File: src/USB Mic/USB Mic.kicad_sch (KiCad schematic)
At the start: 12 parts, among them IC1 ADUM3160BRWZ-RL, J1 GT-USB-7010ASV

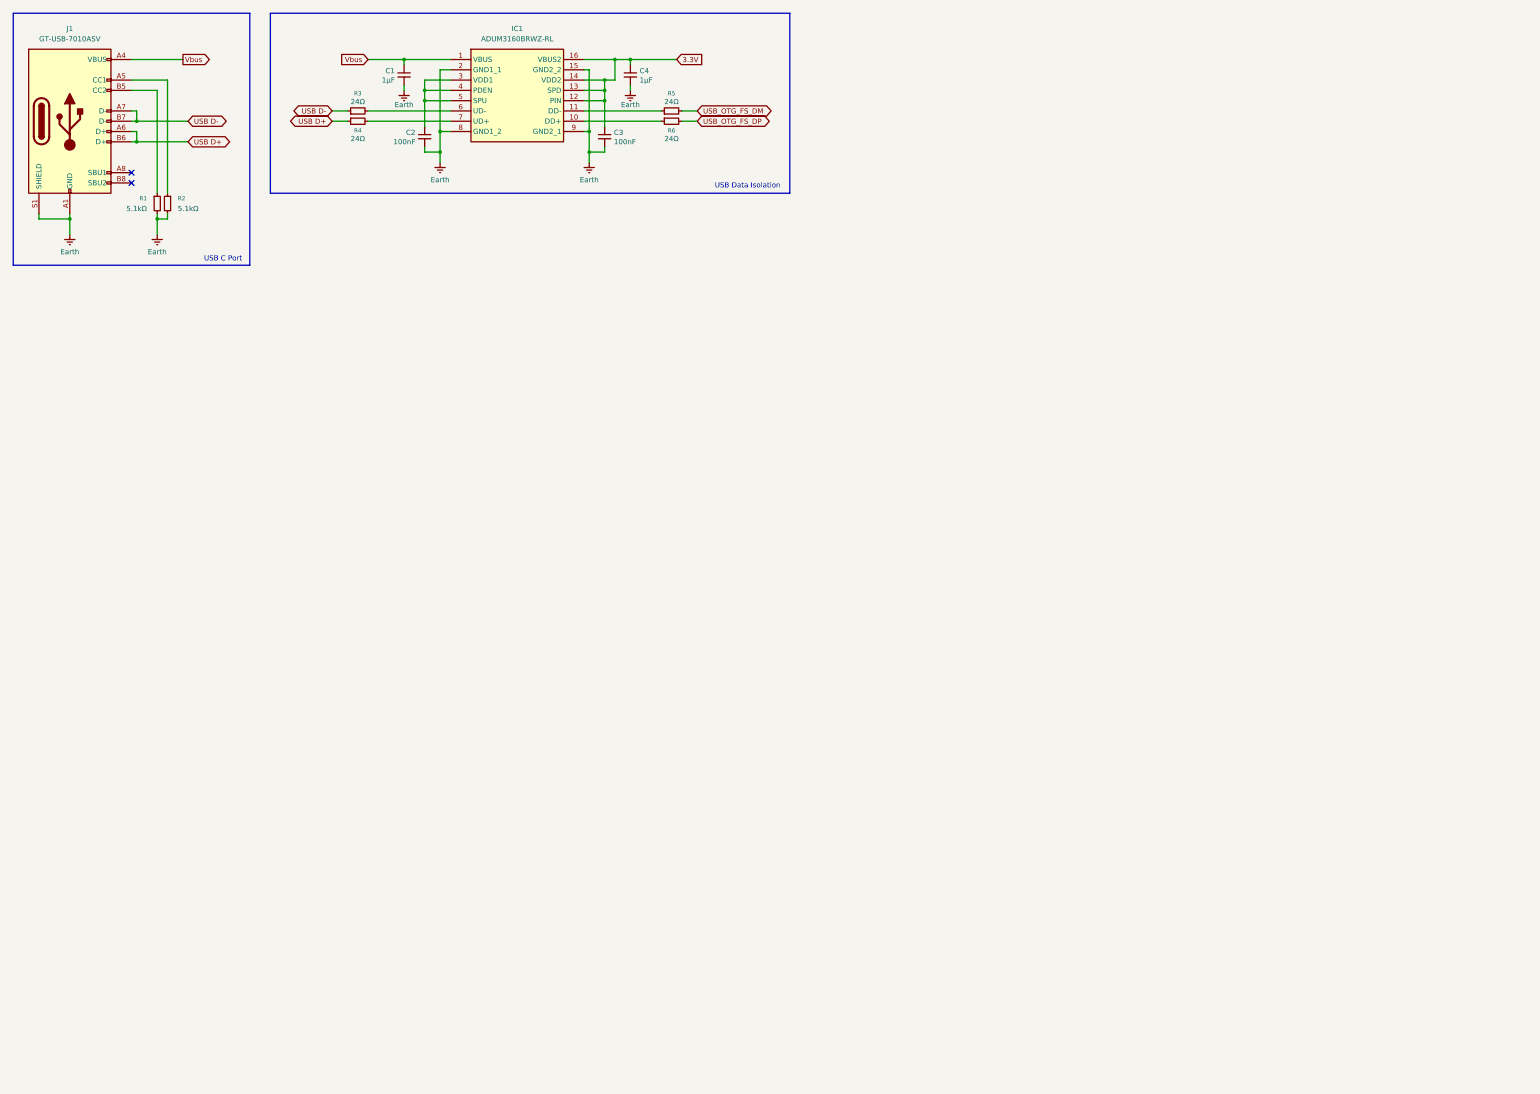
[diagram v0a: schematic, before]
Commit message: Update Rev.4 Schematic
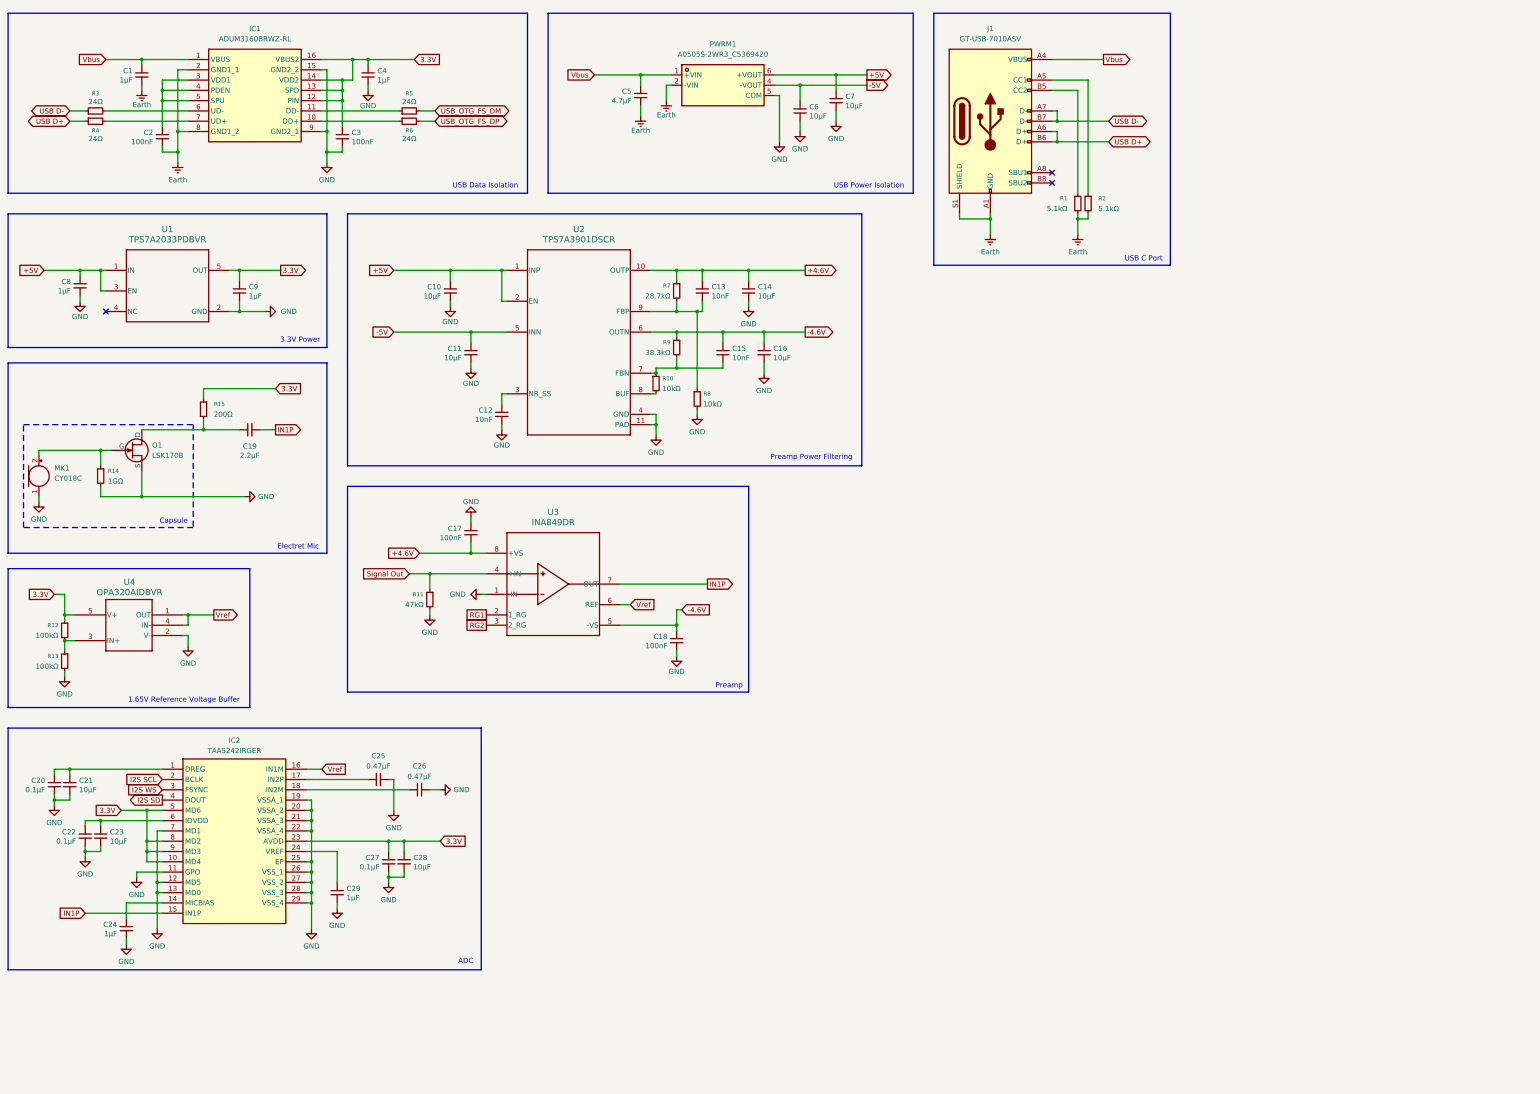
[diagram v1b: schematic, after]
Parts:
- added C10, C11, C14, C16, C21, C23, C28, C6, C7: 10µF, symbol Device:C_Small
- added C12, C13, C15: 10nF, symbol Device:C_Small
- added C17, C18: 100nF, symbol Device:C_Small
- added C19: 2.2µF, symbol Device:C_Small
- added C20, C22, C27: 0.1µF, symbol Device:C_Small
- added C24, C29, C8, C9: 1µF, symbol Device:C_Small
- added C25, C26: 0.47µF, symbol Device:C_Small
- added C5: 4.7µF, symbol Device:C_Small
- added IC2: TAA5242IRGER, footprints:TAA5242IRGER, symbol TAA5242IRGER:TAA5242IRGER
- added MK1: CY018C, symbol Device:Microphone
- added PWRM1: A0505S-2WR3_C5369420, easyeda2kicad:PWRM-TH_HLK-AXXXXS-2WR3, symbol A0505S-2WR3:A0505S-2WR3_C5369420
- added Q1: LSK170B, symbol Simulation_SPICE:NJFET
- added R10, R8: 10kΩ, symbol Device:R_Small
- added R11: 47kΩ, symbol Device:R_Small
- added R12, R13: 100kΩ, symbol Device:R_Small
- added R14: 1GΩ, symbol Device:R_Small
- added R15: 200Ω, symbol Device:R_Small
- added R7: 28.7kΩ, symbol Device:R_Small
- added R9: 38.3kΩ, symbol Device:R_Small
- added U1: TPS7A2033PDBVR, footprints:DBV0005A-IPC_A, symbol TPS7A2033PDBVR:TPS7A2033PDBVR
- added U2: TPS7A3901DSCR, footprints:DSC0010J_NV, symbol TPS7A3901DSCR:TPS7A3901DSCR
- added U3: INA849DR, D0008A-IPC_A, symbol INA849DR:INA849DR
- added U4: OPA320AIDBVR, footprints:DBV5, symbol OPA320AIDBVR:OPA320AIDBVR
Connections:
- net 3.3V: now also C27.1, C28.1, C9.1, IC2.10 (MD4), IC2.23 (AVDD), IC2.5 (MD6), IC2.8 (MD2), IC2.9 (MD3), R12.1, R15.1, U1.5 (OUT), U4.5 (V+)
- net Earth: now also C5.2, PWRM1.2 (-VIN); no longer C3.2, C4.2, IC1.15 (GND2_2), IC1.9 (GND2_1)
- net Vbus: now also C5.1, PWRM1.1 (+VIN)
- new net: C15.2, R10.1, R9.2, U2.7 (FBN)
- new net: R10.2, U2.8 (BUF)
- new net: C12.1, U2.3 (NR_SS)
- new net: C29.1, IC2.24 (VREF)
- new net: MK1.2 (+), Q1.2 (G), R14.1
- new net: C13.2, R7.2, R8.1, U2.9 (FBP)
- new net: C25.1, IC2.17 (IN2P)
- new net: C20.1, C21.1, IC2.1 (DREG)
- new net: C22.1, C23.1, IC2.6 (IOVDD)
- new net: C24.1, IC2.14 (MICBIAS)
- new net: C26.2, IC2.18 (IN2M)
- new net: R12.2, R13.1, U4.3 (IN+)
- new net: C19.1, Q1.1 (D), R15.2
- new net +4.6V: C13.1, C14.1, C17.2, R7.1, U2.10 (OUTP), U3.8 (+VS)
- new net +5V: C10.1, C7.1, C8.1, PWRM1.6 (+VOUT), U1.1 (IN), U1.3 (EN), U2.1 (INP), U2.2 (EN)
- new net -4.6V: C15.1, C16.1, C18.1, R9.1, U2.6 (OUTN), U3.5 (-VS)
- new net -5V: C11.1, C6.1, PWRM1.4 (-VOUT), U2.5 (INN)
- new net GND: C10.2, C11.2, C12.2, C14.2, C16.2, C17.1, C18.2, C20.2, C21.2, C22.2, C23.2, C24.2, C25.2, C26.1, C27.2, C28.2, C29.2, C3.2, C4.2, C6.2, C7.2, C8.2, C9.2, IC1.15 (GND2_2), IC1.9 (GND2_1), IC2.11 (GPO), IC2.12 (MD5), IC2.13 (MD0), IC2.19 (VSSA_1), IC2.20 (VSSA_2), IC2.21 (VSSA_3), IC2.22 (VSSA_4), IC2.25 (EP), IC2.26 (VSS_1), IC2.27 (VSS_2), IC2.28 (VSS_3), IC2.29 (VSS_4), IC2.7 (MD1), MK1.1 (-), PWRM1.5 (COM), Q1.3 (S), R11.2, R13.2, R14.2, R8.2, U1.2 (GND), U2.11 (PAD), U2.4 (GND), U3.1 (-IN), U4.2 (V-)
- new net I2S SCL: IC2.2 (BCLK)
- new net I2S SD: IC2.4 (DOUT)
- new net I2S WS: IC2.3 (FSYNC)
- new net IN1P: C19.2, IC2.15 (IN1P), U3.7 (OUT)
- new net RG1: U3.2 (1_RG)
- new net RG2: U3.3 (2_RG)
- new net Signal Out: R11.1, U3.4 (+IN)
- new net Vref: IC2.16 (IN1M), U3.6 (REF), U4.1 (OUT), U4.4 (IN-)
- no-connect marks 2 -> 3
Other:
- note added: "1.65V Reference Voltage Buffer"
- note added: "3.3V Power"
- note added: "ADC"
- note added: "Capsule"
- note added: "Electret Mic"
- note added: "Preamp"
- note added: "Preamp Power Filtering"
- note added: "USB Power Isolation"
- moved on the sheet: C1, C2, C3, C4, IC1, J1, R1, R2, R3, R4, R5, R6

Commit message: Upload SPICE and update schematic
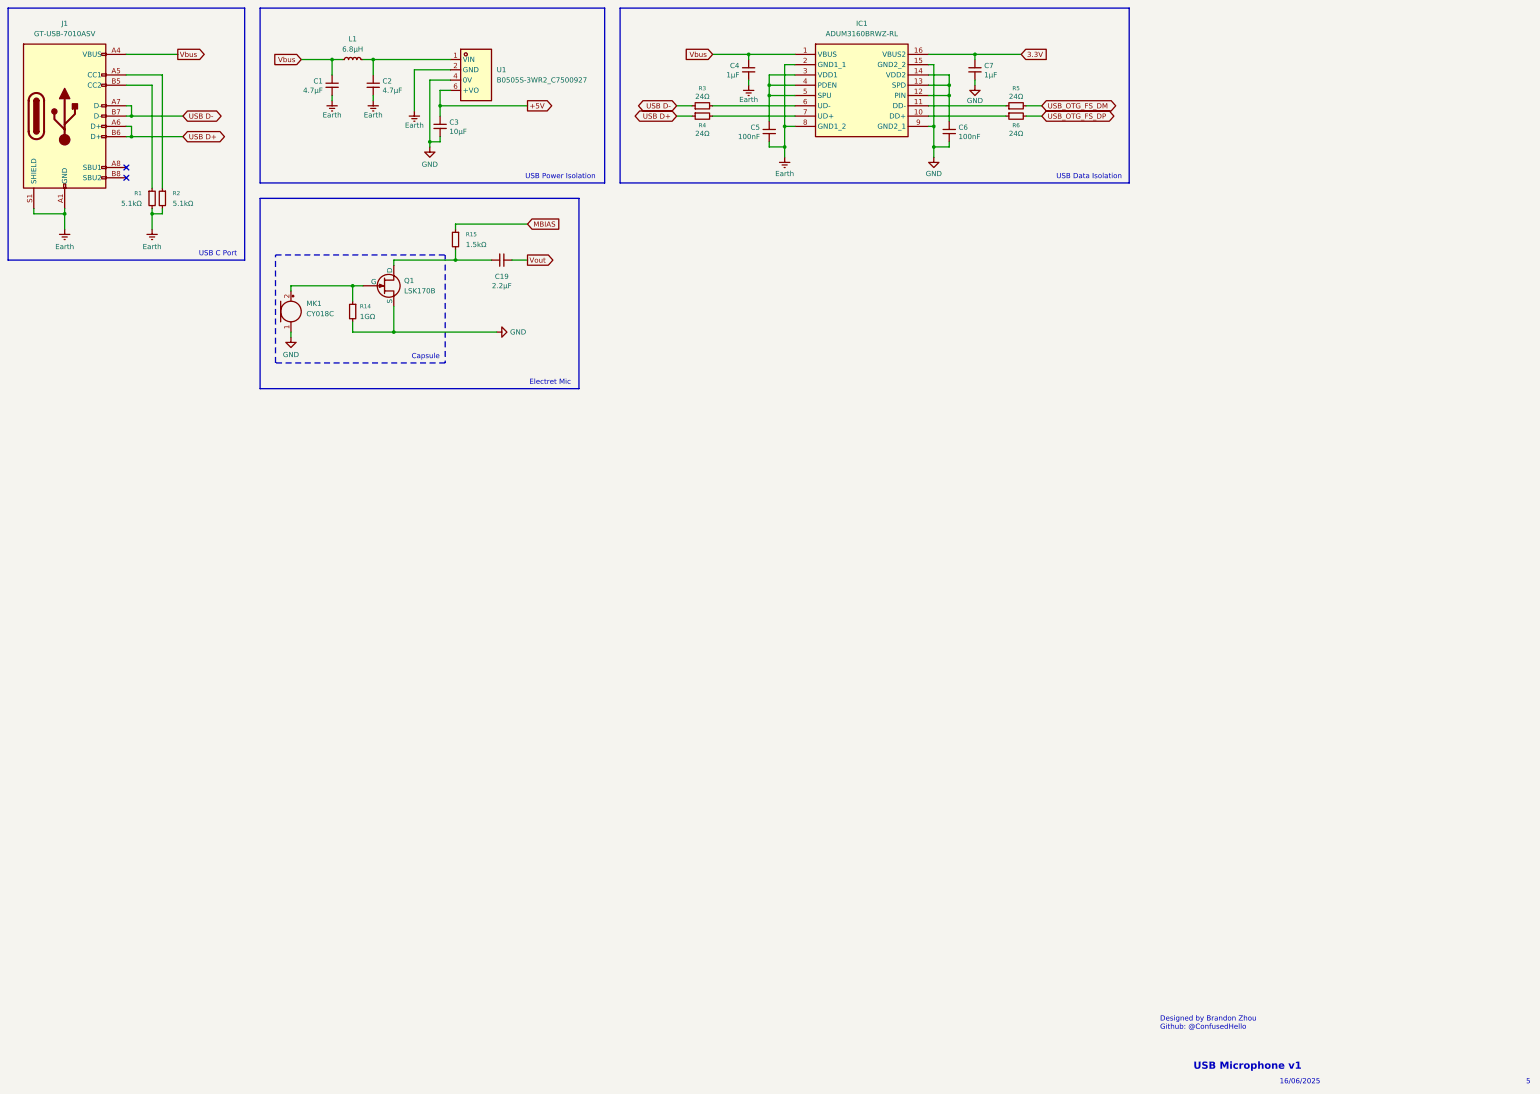
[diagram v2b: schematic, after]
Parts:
- removed C1, C24, C29, C8, C9: 1µF, symbol Device:C_Small
- removed C10, C11, C14, C16, C21, C23, C28, C7: 10µF, symbol Device:C_Small
- removed C12, C13, C15: 10nF, symbol Device:C_Small
- removed C17, C18: 100nF, symbol Device:C_Small
- removed C20, C22, C27: 0.1µF, symbol Device:C_Small
- removed C25, C26: 0.47µF, symbol Device:C_Small
- removed IC2: TAA5242IRGER, footprints:TAA5242IRGER, symbol TAA5242IRGER:TAA5242IRGER
- removed PWRM1: A0505S-2WR3_C5369420, easyeda2kicad:PWRM-TH_HLK-AXXXXS-2WR3, symbol A0505S-2WR3:A0505S-2WR3_C5369420
- removed R10, R8: 10kΩ, symbol Device:R_Small
- removed R11: 47kΩ, symbol Device:R_Small
- removed R12, R13: 100kΩ, symbol Device:R_Small
- removed R7: 28.7kΩ, symbol Device:R_Small
- removed R9: 38.3kΩ, symbol Device:R_Small
- removed U1: TPS7A2033PDBVR, footprints:DBV0005A-IPC_A, symbol TPS7A2033PDBVR:TPS7A2033PDBVR
- removed U2: TPS7A3901DSCR, footprints:DSC0010J_NV, symbol TPS7A3901DSCR:TPS7A3901DSCR
- removed U3: INA849DR, D0008A-IPC_A, symbol INA849DR:INA849DR
- removed U4: OPA320AIDBVR, footprints:DBV5, symbol OPA320AIDBVR:OPA320AIDBVR
- added C4: 1µF, symbol Device:C_Small
- added C5: 100nF, symbol Device:C_Small
- added L1: 6.8µH, footprints:IND-SMD_L4.0-W4.0_YHNR4020, symbol Device:L_Small
- added U1: B0505S-3WR2_C7500927, easyeda2kicad:PWRM-TH_BXXXXS-3WR2, symbol B0505S-3WR2:B0505S-3WR2_C7500927
- C2: value 100nF -> 4.7µF
- C3: value 100nF -> 10µF
- C6: value 10µF -> 100nF
- R15: value 200Ω -> 1.5kΩ
- renumbered C5 to C1, C4 to C7
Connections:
- net +5V: now also C3.1, U1.6 (+VO)
- net 3.3V: no longer C3.1, IC1.12 (PIN), IC1.13 (SPD), IC1.14 (VDD2), R15.1
- net Earth: now also C4.2, C5.2, U1.2 (GND)
- net GND: now also U1.4 (0V)
- net Vbus: now also C4.1, L1.1
- net at IC1.3 (VDD1), IC1.4 (PDEN), IC1.5 (SPU): now also C5.1; no longer C2.1
- net -5V: no longer names the net of C6.1
- net -5V: now also IC1.12 (PIN), IC1.13 (SPD), IC1.14 (VDD2)
- net IN1P renamed Vout
- new net: C2.1, L1.2, U1.1 (VIN)
- new net MBIAS: R15.1
- no-connect marks 3 -> 2
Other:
- note added: "16/06/2025"
- note added: "5"
- note added: "Designed by Brandon Zhou Github: @ConfusedHello"
- note added: "USB Microphone v1"
- note removed: "1.65V Reference Voltage Buffer"
- note removed: "3.3V Power"
- note removed: "ADC"
- note removed: "Preamp"
- note removed: "Preamp Power Filtering"
- moved on the sheet: C1, C19, C7, IC1, J1, MK1, Q1, R1, R14, R15, R2, R3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

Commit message: Update to Rev. 5
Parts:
- removed C19: 2.2µF, symbol Device:C_Small
- removed R14: 1GΩ, symbol Device:R_Small
- removed R15: 1.5kΩ, symbol Device:R_Small
- added C10, C11: 10nF, symbol Device:C_Small
- added C12, C13, C8, C9: 22µF, symbol Device:C_Small
- added C14: 2.2µF, symbol Device:C_Small
- added IC2: TPS7A8901RTJR, footprints:QFN50P400X400X80-21N-D, symbol TPS7A8901RTJR:TPS7A8901RTJR
- added R10: 33.2kΩ, symbol Device:R_Small
- added R11: 1GΩ, symbol Device:R_Small
- added R12: 400Ω, symbol Device:R_Small
- added R7: 10kΩ, symbol Device:R_Small
- added R8: 47.5kΩ, symbol Device:R_Small
- added R9: 10.7kΩ, symbol Device:R_Small
- Q1: value LSK170B -> J305
- U1: footprint easyeda2kicad:PWRM-TH_BXXXXS-3WR2 -> footprints:B0505S-3WR2
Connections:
- net +5V: now also C8.1, C9.1, IC2.1 (IN1_1), IC2.2 (IN1_2), IC2.20 (EN1), IC2.4 (IN2_1), IC2.5 (IN2_2), IC2.6 (EN2)
- net 3.3V: now also C6.1, IC1.12 (PIN), IC1.13 (SPD), IC1.14 (VDD2), C13.1, IC2.11 (OUT2_1), IC2.12 (OUT2_2), R10.2
- net GND: now also C10.1, C11.2, C12.1, C13.2, C8.2, C9.2, IC2.13 (GND_2), IC2.18 (SS_CTRL1), IC2.21 (EP), IC2.7 (NR/SS2), R11.2, R7.1, R9.2
- net at MK1.2 (+), Q1.2 (G): now also R11.1
- net at Q1.1 (D): now also C14.1, R12.2
- net USB_OTG_FS_DM renamed USB_FS_DM
- net USB_OTG_FS_DP renamed USB_FS_DP
- new net: IC2.10 (FB2), R10.1, R9.1
- new net: C10.2, IC2.19 (NR/SS1)
- new net: IC2.16 (FB1), R7.2, R8.1
- new net: C11.1, IC2.8 (SS_CTRL2)
- new net 4.6V: C12.2, IC2.14 (OUT1_1), IC2.15 (OUT1_2), R12.1, R8.2
- new net Capsule Signal: C14.2
- no-connect marks 2 -> 4
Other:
- note added: "LDO Power Filtering"
- moved on the sheet: C4, C5, C6, C7, IC1, MK1, Q1, R3, R4, R5, R6
